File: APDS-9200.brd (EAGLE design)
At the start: 15.2 x 7.6 mm, 12 parts

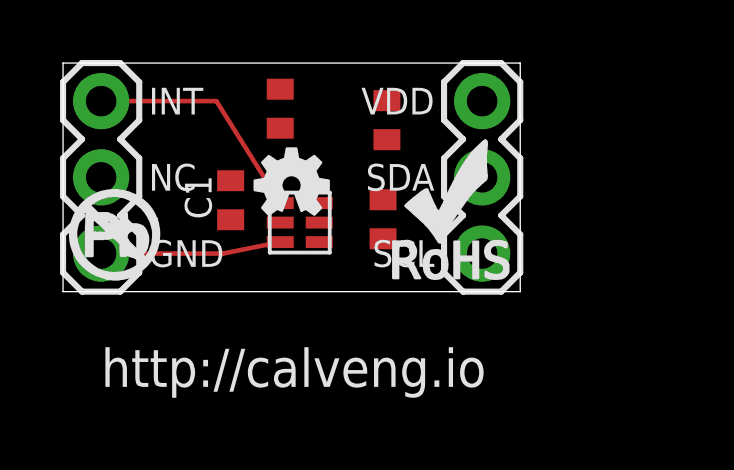
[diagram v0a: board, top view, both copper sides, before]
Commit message: Fixed on board labels
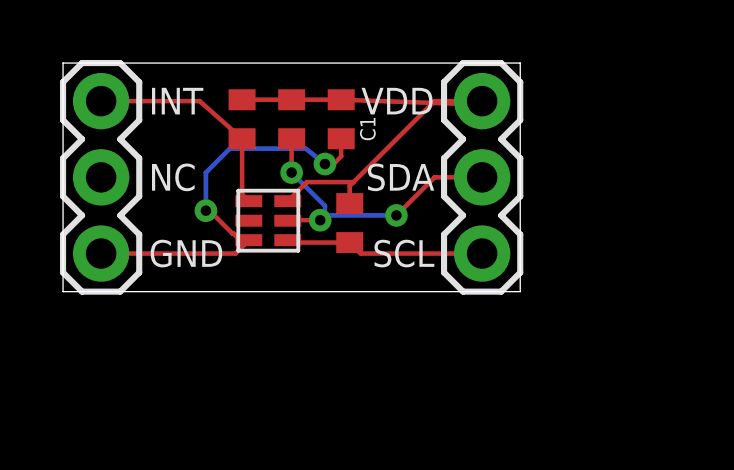
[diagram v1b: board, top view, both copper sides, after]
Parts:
- removed LOGO2: NO_PB_LOGO, CalvEngIO-Logos:NO_PB_LOGO_0.120
- removed LOGO3: ROHS_LOGO, CalvEngIO-Logos:ROHS_LOGO_0.18_IN
- removed U$2: WEBSITE.05, CalvEngIO-Logos:WEBSITE.05
- C1: value (none) -> 1uF
- R1, R2, R3: value (none) -> 10k
- moved C1 4.57 mm to (9.27, 5.75)
- moved R1 3.18 mm to (7.62, 5.75)
- moved R3 1.32 mm to (5.97, 5.75)
- moved R2 1.12 mm to (9.56, 2.29)
- moved APDS-1 1.05 mm to (7.84, 3.37)
- moved U$1 0.35 mm to (7.30, 1.59)
- flipped LOGO1 to the bottom
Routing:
- net N$1: track 0.00 -> 16.7 mm
- net N$4: track 0.00 -> 10.1 mm, vias 0 -> 3
- net N$2: track 6.01 -> 13.8 mm, vias 0 -> 2
- net N$5: track 0.00 -> 6.66 mm
- net N$3: track 7.85 -> 7.35 mm

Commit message: Fixed on board labels
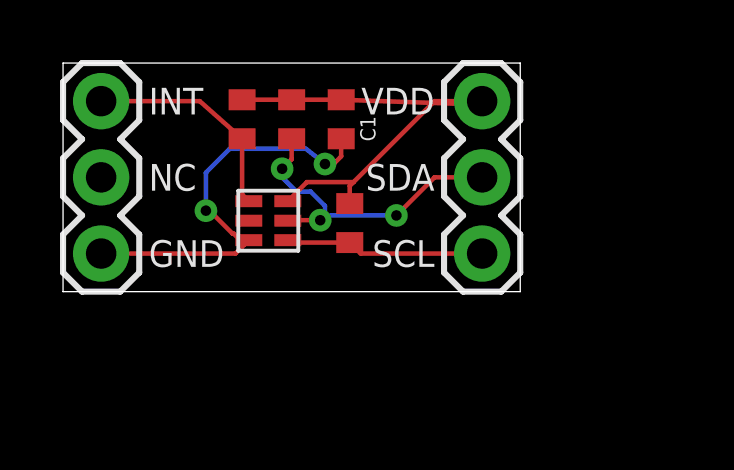
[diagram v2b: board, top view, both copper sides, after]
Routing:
- net N$4: track 10.1 -> 10.6 mm
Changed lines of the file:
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@@
 <wire x1="7.508" y1="2.38125" x2="7.49225" y2="2.3655" width="0.1524" layer="1"/>
 <wire x1="12.3825" y1="3.81" x2="11.1125" y2="2.54" width="0.1524" layer="1"/>
-<wire x1="7.62" y1="5.09675" x2="7.62" y2="3.96875" width="0.1524" layer="1"/>
-<via x="7.62" y="3.96875" extent="1-16" drill="0.35"/>
-<wire x1="7.62" y1="3.96875" x2="8.73125" y2="2.8575" width="0.1524" layer="16"/>
+<via x="7.3025" y="4.09575" extent="1-16" drill="0.35"/>
 <wire x1="8.73125" y1="2.8575" x2="8.73125" y2="2.54" width="0.1524" layer="16"/>
+<wire x1="7.62" y1="5.09675" x2="7.62" y2="4.41325" width="0.1524" layer="1"/>
+<wire x1="7.62" y1="4.41325" x2="7.3025" y2="4.09575" width="0.1524" layer="1"/>
+<wire x1="7.3025" y1="4.09575" x2="7.3025" y2="3.81" width="0.1524" layer="16"/>
+<wire x1="7.3025" y1="3.81" x2="7.77875" y2="3.33375" width="0.1524" layer="16"/>
+<wire x1="7.77875" y1="3.33375" x2="8.255" y2="3.33375" width="0.1524" layer="16"/>
+<wire x1="8.255" y1="3.33375" x2="8.73125" y2="2.8575" width="0.1524" layer="16"/>
 </signal>
 <signal name="N$5">
